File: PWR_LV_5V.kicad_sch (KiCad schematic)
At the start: 14 parts, among them IC1 LMR51460SQDRRRQ1

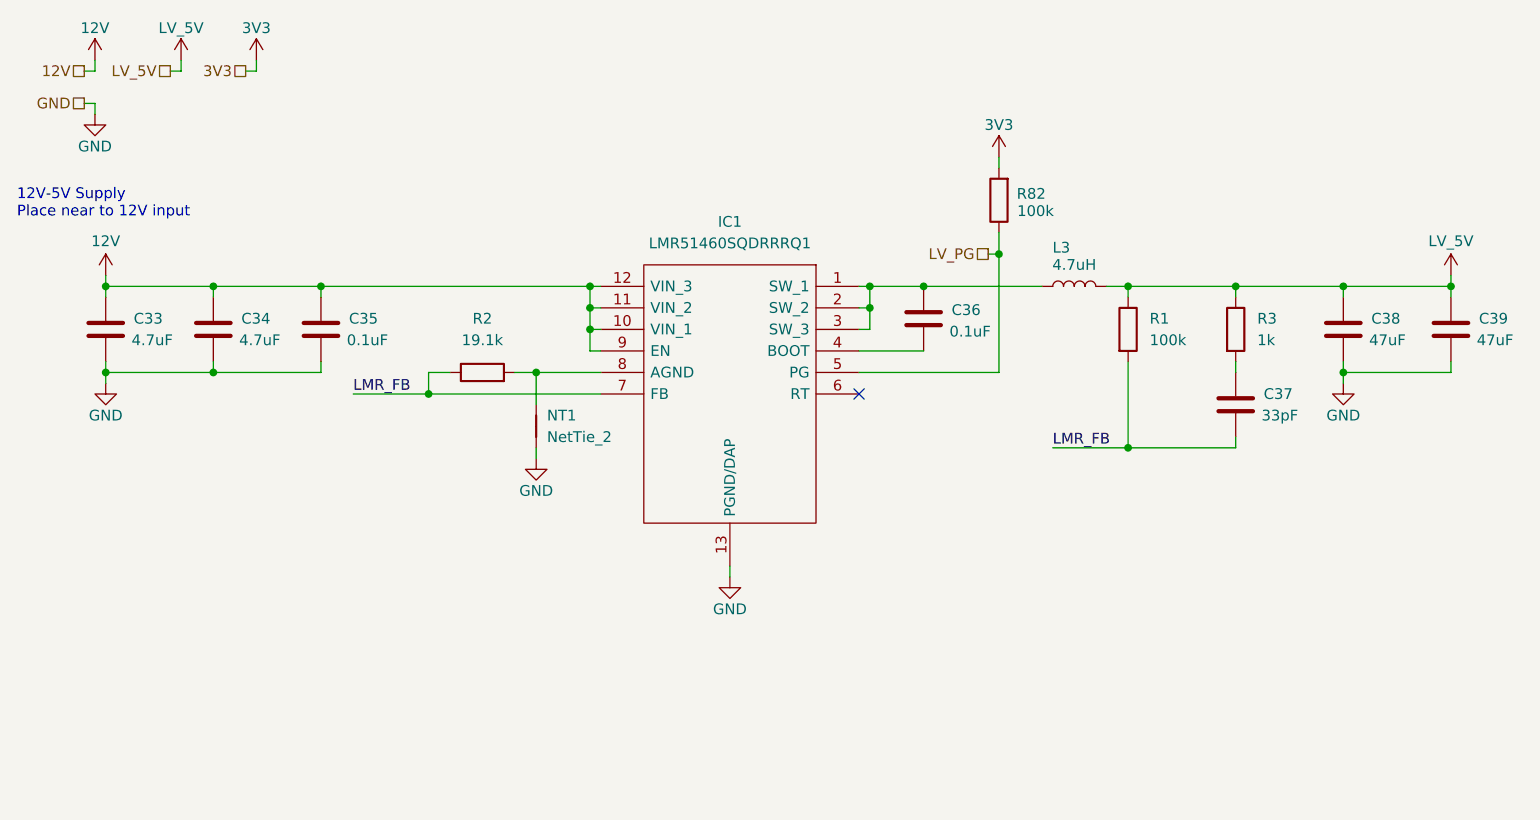
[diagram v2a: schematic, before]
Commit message: finished initial esp routing
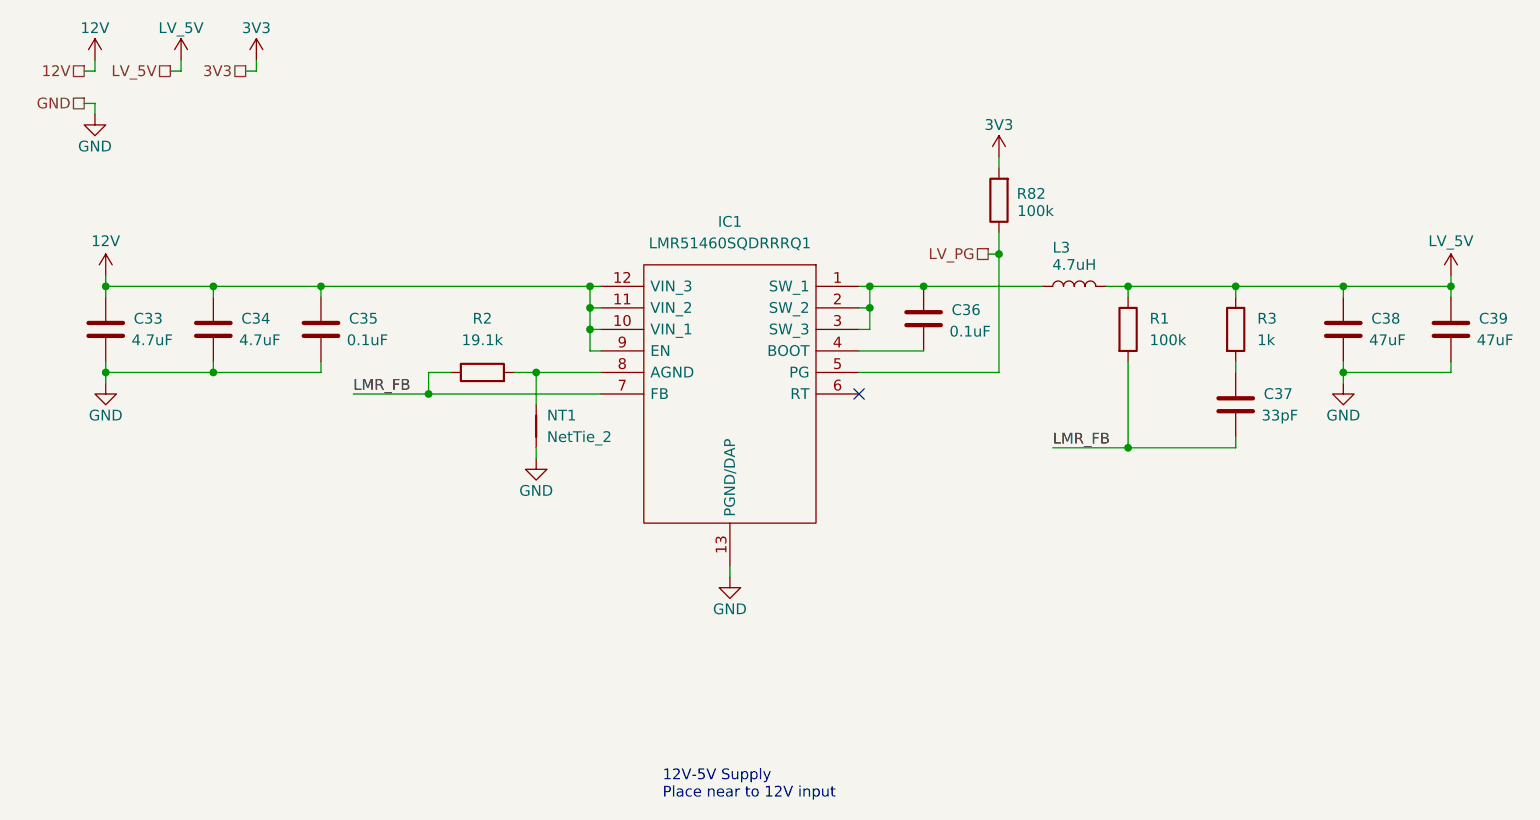
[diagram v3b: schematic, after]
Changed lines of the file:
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@@
 	(text_box "12V-5V Supply\nPlace near to 12V input"
 		(exclude_from_sim no)
-		(at 13.97 35.56 0)
+		(at 90.17 104.14 0)
 		(size 30.48 6.35)
 		(margins 0.9525 0.9525 0.9525 0.9525)

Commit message: redid annotations, added test point
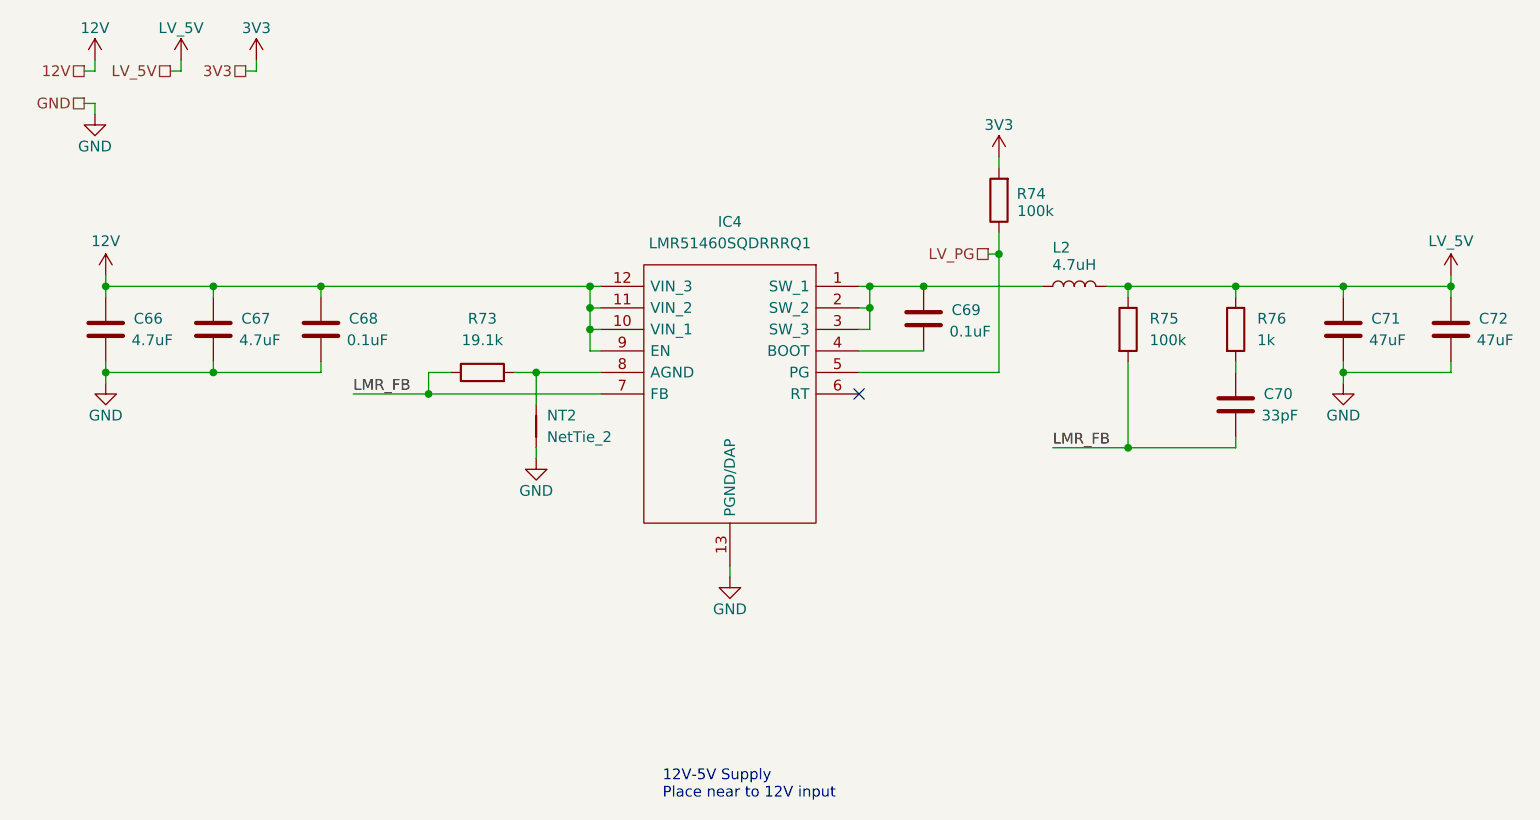
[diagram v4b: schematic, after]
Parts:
- renumbered C33 to C66, C34 to C67, C35 to C68, C36 to C69, C37 to C70, C38 to C71, C39 to C72, IC1 to IC4, L3 to L2, NT1 to NT2, R2 to R73, R82 to R74, R1 to R75, R3 to R76
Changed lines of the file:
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@@
 		(dnp no)
 		(fields_autoplaced yes)
-		(property "Reference" "R3"
+		(property "Reference" "R76"
 			(at 161.29 52.0699 0)
 			(effects
@@
 			(project "NCU"
 				(path "/3aee14c3-5480-4f7c-989e-3fef81779034/05e3be97-98f6-4518-a1a7-240d4da327e6/55c548c3-ff9a-4db1-af94-bd7e8aa4e38e"
-					(reference "R3")
+					(reference "R76")
 					(unit 1)
 				)
@@
 		(dnp no)
 		(fields_autoplaced yes)
-		(property "Reference" "R2"
+		(property "Reference" "R73"
 			(at 69.85 52.07 90)
 			(effects
@@
 			(project "NCU"
 				(path "/3aee14c3-5480-4f7c-989e-3fef81779034/05e3be97-98f6-4518-a1a7-240d4da327e6/55c548c3-ff9a-4db1-af94-bd7e8aa4e38e"
-					(reference "R2")
+					(reference "R73")
 					(unit 1)
 				)
@@
 		(on_board yes)
 		(dnp no)
-		(property "Reference" "C34"
+		(property "Reference" "C67"
 			(at 41.402 52.07 0)
 			(effects
@@
 			(project "NCU"
 				(path "/3aee14c3-5480-4f7c-989e-3fef81779034/05e3be97-98f6-4518-a1a7-240d4da327e6/55c548c3-ff9a-4db1-af94-bd7e8aa4e38e"
-					(reference "C34")
+					(reference "C67")
 					(unit 1)
 				)
@@
 		(on_board yes)
 		(dnp no)
-		(property "Reference" "C35"
+		(property "Reference" "C68"
 			(at 54.102 52.07 0)
 			(effects
@@
 			(project "NCU"
 				(path "/3aee14c3-5480-4f7c-989e-3fef81779034/05e3be97-98f6-4518-a1a7-240d4da327e6/55c548c3-ff9a-4db1-af94-bd7e8aa4e38e"
-					(reference "C35")
+					(reference "C68")
 					(unit 1)
 				)
@@
 		(on_board yes)
 		(dnp no)
-		(property "Reference" "C38"
+		(property "Reference" "C71"
 			(at 174.752 52.07 0)
 			(effects
@@
 			(project "NCU"
 				(path "/3aee14c3-5480-4f7c-989e-3fef81779034/05e3be97-98f6-4518-a1a7-240d4da327e6/55c548c3-ff9a-4db1-af94-bd7e8aa4e38e"
-					(reference "C38")
+					(reference "C71")
 					(unit 1)
 				)
@@
 		(on_board yes)
 		(dnp no)
-		(property "Reference" "IC1"
+		(property "Reference" "IC4"
 			(at 99.06 40.64 0)
 			(effects
@@
 			(project "NCU"
 				(path "/3aee14c3-5480-4f7c-989e-3fef81779034/05e3be97-98f6-4518-a1a7-240d4da327e6/55c548c3-ff9a-4db1-af94-bd7e8aa4e38e"
-					(reference "IC1")
+					(reference "IC4")
 					(unit 1)
 				)
@@
 		(on_board yes)
 		(dnp no)
-		(property "Reference" "L3"
+		(property "Reference" "L2"
 			(at 138.176 43.688 90)
 			(effects
@@
 			(project "NCU"
 				(path "/3aee14c3-5480-4f7c-989e-3fef81779034/05e3be97-98f6-4518-a1a7-240d4da327e6/55c548c3-ff9a-4db1-af94-bd7e8aa4e38e"
-					(reference "L3")
+					(reference "L2")
 					(unit 1)
 				)
@@
 		(on_board yes)
 		(dnp no)
-		(property "Reference" "#PWR052"
+		(property "Reference" "#PWR0270"
 			(at 76.2 74.93 0)
 			(effects
@@
 			(project "NCU"
 				(path "/3aee14c3-5480-4f7c-989e-3fef81779034/05e3be97-98f6-4518-a1a7-240d4da327e6/55c548c3-ff9a-4db1-af94-bd7e8aa4e38e"
-					(reference "#PWR052")
+					(reference "#PWR0270")
 					(unit 1)
 				)
@@
 		(dnp no)
 		(fields_autoplaced yes)
-		(property "Reference" "R1"
+		(property "Reference" "R75"
 			(at 148.59 52.0699 0)
 			(effects
@@
 			(project "NCU"
 				(path "/3aee14c3-5480-4f7c-989e-3fef81779034/05e3be97-98f6-4518-a1a7-240d4da327e6/55c548c3-ff9a-4db1-af94-bd7e8aa4e38e"
-					(reference "R1")
+					(reference "R75")
 					(unit 1)
 				)
@@
 		(dnp no)
 		(fields_autoplaced yes)
-		(property "Reference" "NT1"
+		(property "Reference" "NT2"
 			(at 77.47 63.4999 90)
 			(effects
@@
 			(project "NCU"
 				(path "/3aee14c3-5480-4f7c-989e-3fef81779034/05e3be97-98f6-4518-a1a7-240d4da327e6/55c548c3-ff9a-4db1-af94-bd7e8aa4e38e"
-					(reference "NT1")
+					(reference "NT2")
 					(unit 1)
 				)
@@
 		(on_board yes)
 		(dnp no)
-		(property "Reference" "#PWR053"
+		(property "Reference" "#PWR0273"
 			(at 171.45 66.04 0)
 			(effects
@@
 			(project "NCU"
 				(path "/3aee14c3-5480-4f7c-989e-3fef81779034/05e3be97-98f6-4518-a1a7-240d4da327e6/55c548c3-ff9a-4db1-af94-bd7e8aa4e38e"
-					(reference "#PWR053")
+					(reference "#PWR0273")
 					(unit 1)
 				)
@@
 		(on_board yes)
 		(dnp no)
-		(property "Reference" "C37"
+		(property "Reference" "C70"
 			(at 162.052 60.96 0)
 			(effects
@@
 			(project "NCU"
 				(path "/3aee14c3-5480-4f7c-989e-3fef81779034/05e3be97-98f6-4518-a1a7-240d4da327e6/55c548c3-ff9a-4db1-af94-bd7e8aa4e38e"
-					(reference "C37")
+					(reference "C70")
 					(unit 1)
 				)
@@
 		(on_board yes)
 		(dnp no)
-		(property "Reference" "#PWR0261"
+		(property "Reference" "#PWR0264"
 			(at 24.13 25.4 0)
 			(effects
@@
 			(project "NCU"
 				(path "/3aee14c3-5480-4f7c-989e-3fef81779034/05e3be97-98f6-4518-a1a7-240d4da327e6/55c548c3-ff9a-4db1-af94-bd7e8aa4e38e"
-					(reference "#PWR0261")
+					(reference "#PWR0264")
 					(unit 1)
 				)
@@
 		(on_board yes)
 		(dnp no)
-		(property "Reference" "C36"
+		(property "Reference" "C69"
 			(at 125.222 51.054 0)
 			(effects
@@
 			(project "NCU"
 				(path "/3aee14c3-5480-4f7c-989e-3fef81779034/05e3be97-98f6-4518-a1a7-240d4da327e6/55c548c3-ff9a-4db1-af94-bd7e8aa4e38e"
-					(reference "C36")
+					(reference "C69")
 					(unit 1)
 				)
@@
 		(on_board yes)
 		(dnp no)
-		(property "Reference" "#PWR0263"
+		(property "Reference" "#PWR0268"
 			(at 34.29 25.4 0)
 			(effects
@@
 			(project "NCU"
 				(path "/3aee14c3-5480-4f7c-989e-3fef81779034/05e3be97-98f6-4518-a1a7-240d4da327e6/55c548c3-ff9a-4db1-af94-bd7e8aa4e38e"
-					(reference "#PWR0263")
+					(reference "#PWR0268")
 					(unit 1)
 				)
@@
 		(on_board yes)
 		(dnp no)
-		(property "Reference" "#PWR0267"
+		(property "Reference" "#PWR0272"
 			(at 130.81 36.83 0)
 			(effects
@@
 			(project "NCU"
 				(path "/3aee14c3-5480-4f7c-989e-3fef81779034/05e3be97-98f6-4518-a1a7-240d4da327e6/55c548c3-ff9a-4db1-af94-bd7e8aa4e38e"
-					(reference "#PWR0267")
+					(reference "#PWR0272")
 					(unit 1)
 				)
@@
 		(on_board yes)
 		(dnp no)
-		(property "Reference" "#PWR050"
+		(property "Reference" "#PWR0267"
 			(at 25.4 66.04 0)
 			(effects
@@
 			(project "NCU"
 				(path "/3aee14c3-5480-4f7c-989e-3fef81779034/05e3be97-98f6-4518-a1a7-240d4da327e6/55c548c3-ff9a-4db1-af94-bd7e8aa4e38e"
-					(reference "#PWR050")
+					(reference "#PWR0267")
 					(unit 1)
 				)
@@
 		(on_board yes)
 		(dnp no)
-		(property "Reference" "#PWR0262"
+		(property "Reference" "#PWR0265"
 			(at 24.13 34.29 0)
 			(effects
@@
 			(project "NCU"
 				(path "/3aee14c3-5480-4f7c-989e-3fef81779034/05e3be97-98f6-4518-a1a7-240d4da327e6/55c548c3-ff9a-4db1-af94-bd7e8aa4e38e"
-					(reference "#PWR0262")
+					(reference "#PWR0265")
 					(unit 1)
 				)
@@
 		(on_board yes)
 		(dnp no)
-		(property "Reference" "#PWR0266"
+		(property "Reference" "#PWR0269"
 			(at 43.18 25.4 0)
 			(effects
@@
 			(project "NCU"
 				(path "/3aee14c3-5480-4f7c-989e-3fef81779034/05e3be97-98f6-4518-a1a7-240d4da327e6/55c548c3-ff9a-4db1-af94-bd7e8aa4e38e"
-					(reference "#PWR0266")
+					(reference "#PWR0269")
 					(unit 1)
 				)
@@
 		(on_board yes)
 		(dnp no)
-		(property "Reference" "C33"
+		(property "Reference" "C66"
 			(at 28.702 52.07 0)
 			(effects
@@
 			(project "NCU"
 				(path "/3aee14c3-5480-4f7c-989e-3fef81779034/05e3be97-98f6-4518-a1a7-240d4da327e6/55c548c3-ff9a-4db1-af94-bd7e8aa4e38e"
-					(reference "C33")
+					(reference "C66")
 					(unit 1)
 				)
@@
 		(on_board yes)
 		(dnp no)
-		(property "Reference" "C39"
+		(property "Reference" "C72"
 			(at 187.452 52.07 0)
 			(effects
@@
 			(project "NCU"
 				(path "/3aee14c3-5480-4f7c-989e-3fef81779034/05e3be97-98f6-4518-a1a7-240d4da327e6/55c548c3-ff9a-4db1-af94-bd7e8aa4e38e"
-					(reference "C39")
+					(reference "C72")
 					(unit 1)
 				)
@@
 		(on_board yes)
 		(dnp no)
-		(property "Reference" "#PWR054"
+		(property "Reference" "#PWR0274"
 			(at 184.15 50.8 0)
 			(effects
@@
 			(project "NCU"
 				(path "/3aee14c3-5480-4f7c-989e-3fef81779034/05e3be97-98f6-4518-a1a7-240d4da327e6/55c548c3-ff9a-4db1-af94-bd7e8aa4e38e"
-					(reference "#PWR054")
+					(reference "#PWR0274")
 					(unit 1)
 				)
@@
 		(on_board yes)
 		(dnp no)
-		(property "Reference" "#PWR051"
+		(property "Reference" "#PWR0271"
 			(at 99.06 88.9 0)
 			(effects
@@
 			(project "NCU"
 				(path "/3aee14c3-5480-4f7c-989e-3fef81779034/05e3be97-98f6-4518-a1a7-240d4da327e6/55c548c3-ff9a-4db1-af94-bd7e8aa4e38e"
-					(reference "#PWR051")
+					(reference "#PWR0271")
 					(unit 1)
 				)
@@
 		(on_board yes)
 		(dnp no)
-		(property "Reference" "R82"
+		(property "Reference" "R74"
 			(at 134.62 37.338 0)
 			(effects
@@
 			(project "NCU"
 				(path "/3aee14c3-5480-4f7c-989e-3fef81779034/05e3be97-98f6-4518-a1a7-240d4da327e6/55c548c3-ff9a-4db1-af94-bd7e8aa4e38e"
-					(reference "R82")
+					(reference "R74")
 					(unit 1)
 				)
@@
 		(on_board yes)
 		(dnp no)
-		(property "Reference" "#PWR049"
+		(property "Reference" "#PWR0266"
 			(at 25.4 50.8 0)
 			(effects
@@
 			(project "NCU"
 				(path "/3aee14c3-5480-4f7c-989e-3fef81779034/05e3be97-98f6-4518-a1a7-240d4da327e6/55c548c3-ff9a-4db1-af94-bd7e8aa4e38e"
-					(reference "#PWR049")
-					(unit 1)
-				)
+					(reference "#PWR0266")
+					(unit 1)
+				)
